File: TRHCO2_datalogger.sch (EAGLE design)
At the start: 32 parts, among them J3 MicroUSB (5V), U1 ATMEGA328P-MU, U7 SHT31/35, U8 MCP1703/3.3V, Y1 16MHZ

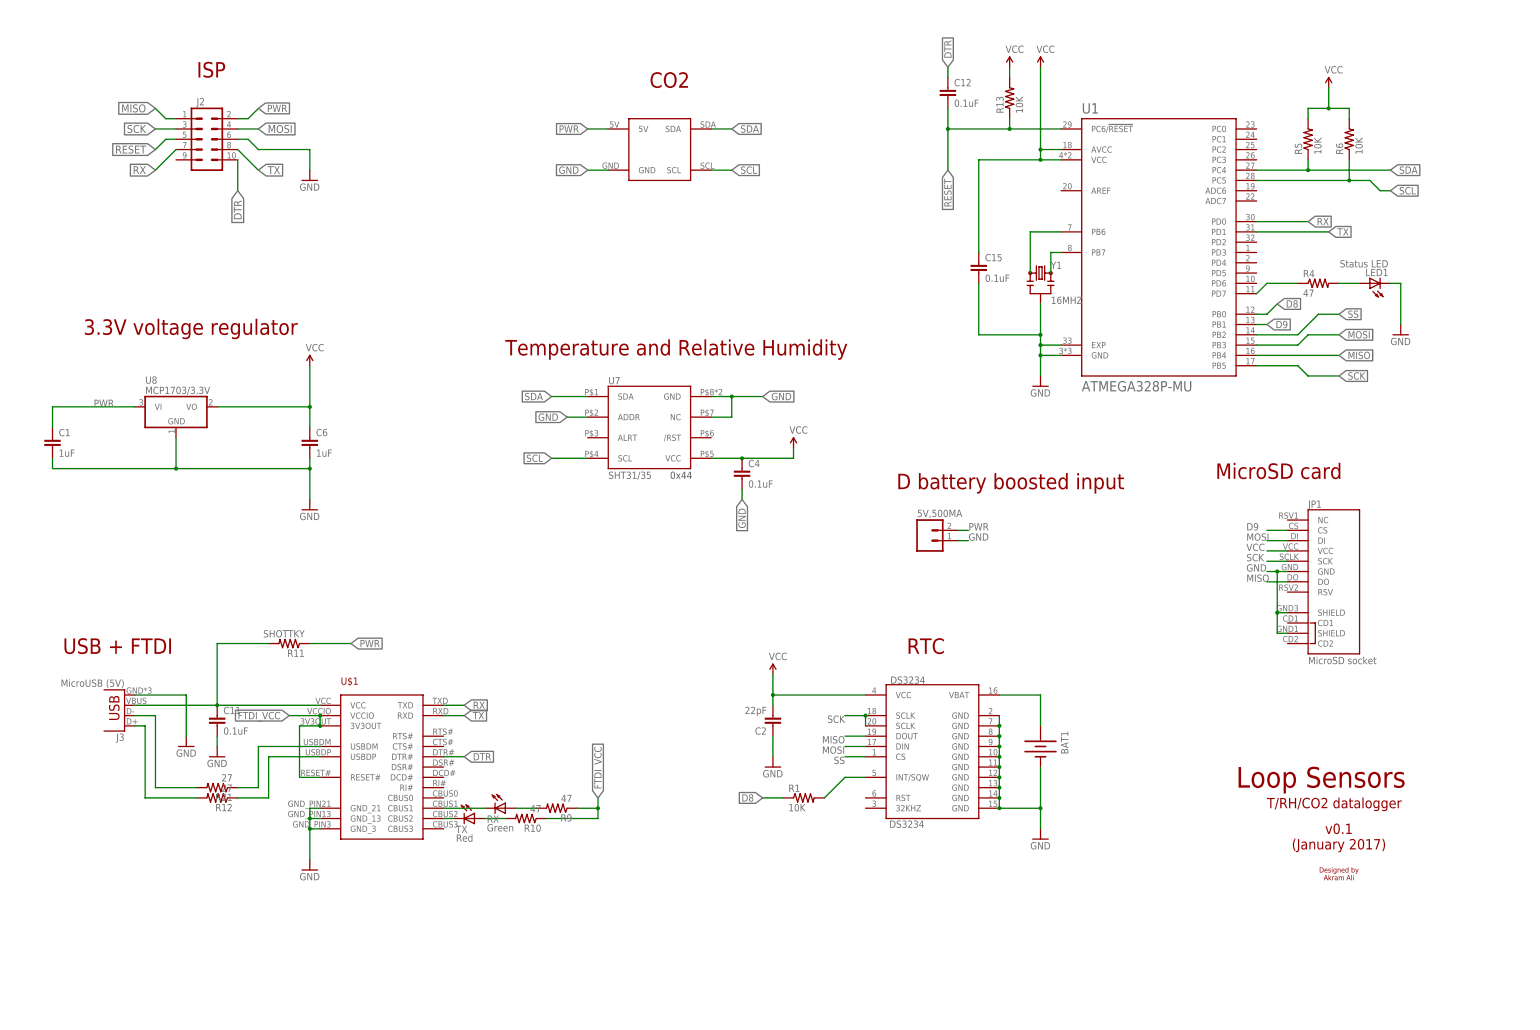
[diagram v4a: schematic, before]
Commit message: v0.2 - Major fixes
- Flipped header for LiPo boost. + and - are now facing up
- Added pullup on DS3234 clock - so there is no interference while
flashing bootloader (can be removed by desoldering jumper)
- Added NPN transistor in the circuit to switch microSD card on/off for
previous adaptations of Sdfat library
- Routed CS pin of microSD card to ISP header for debug when necessary
- Added 1uF capacitor to microSD's supply
- Minor bug fixes and trace rearrangments
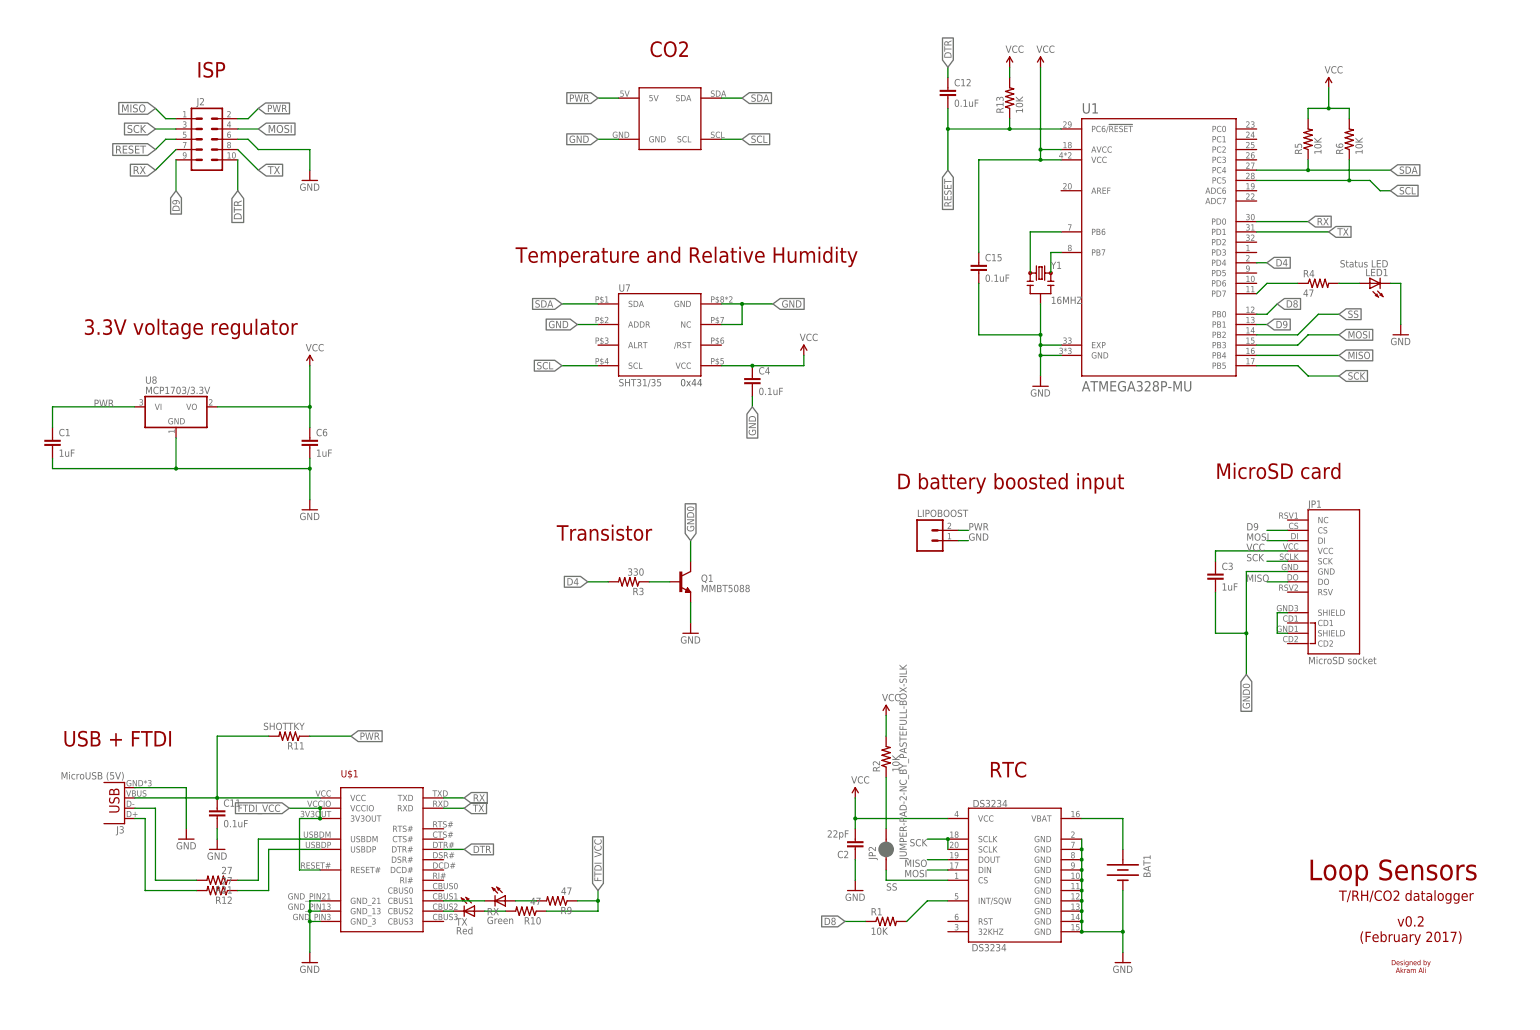
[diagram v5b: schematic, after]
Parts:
- added C3: 1uF, SparkFun-Capacitors:CAP0805
- added JP2: JUMPER-PAD-2-NC_BY_PASTEFULL-BOX-SILK, SparkFun-Passives:JUMPER-PAD-2-NC_BY_PASTEFULL-BOX-SILK
- added Q1: MMBT5088, SparkFun-DiscreteSemi:TRANSISTOR_NPNMMBT5088
- added R2: 10K, SparkFun-Resistors:RESISTOR0805-RES
- added R3: 330, SparkFun-Passives:RESISTOR0805-RES
- renumbered 5V,500MA to LIPOBOOST
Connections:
- new net D4: R3.2, U1.PD4
- new net GND0: C3.2, JP1.GND, Q1.C
- new net N$6: Q1.B, R3.1
- new net N$7: JP2.2, R2.1
- net D9: now also J2.9
- net GND: now also Q1.E; no longer JP1.GND
- net SS: now also JP2.1
- net VCC: now also C3.1, R2.2
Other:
- note added: "Transistor"
- note added: "v0.2 (February 2017)"
- note removed: "v0.1 (January 2017)"
- moved on the sheet: BAT1, C11, C2, C4, DS3234, J3, R1, R10, R11, R12, R21, R9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

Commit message: v0.3 - major update
- Added boost converter (TPS61090)
- Added switch for battery
- Replaced ISP header with TagConnect pins
- Added pullups on all SPI devices
- Removed transistor from sensors and SD card
- Removed jumper @ DS3234 pull up
- Battery groove at edge
- Added LEDs for status indication
- Changed CO2 sensor dimensions to be exact
- Align USB port in center
- Removed PWR LED from booster circuir
- Changed some parts to 0402
- Replaced 16 MHz footprint
- Reroute all traces
- Added LiPo charger circuit (MCP73871)
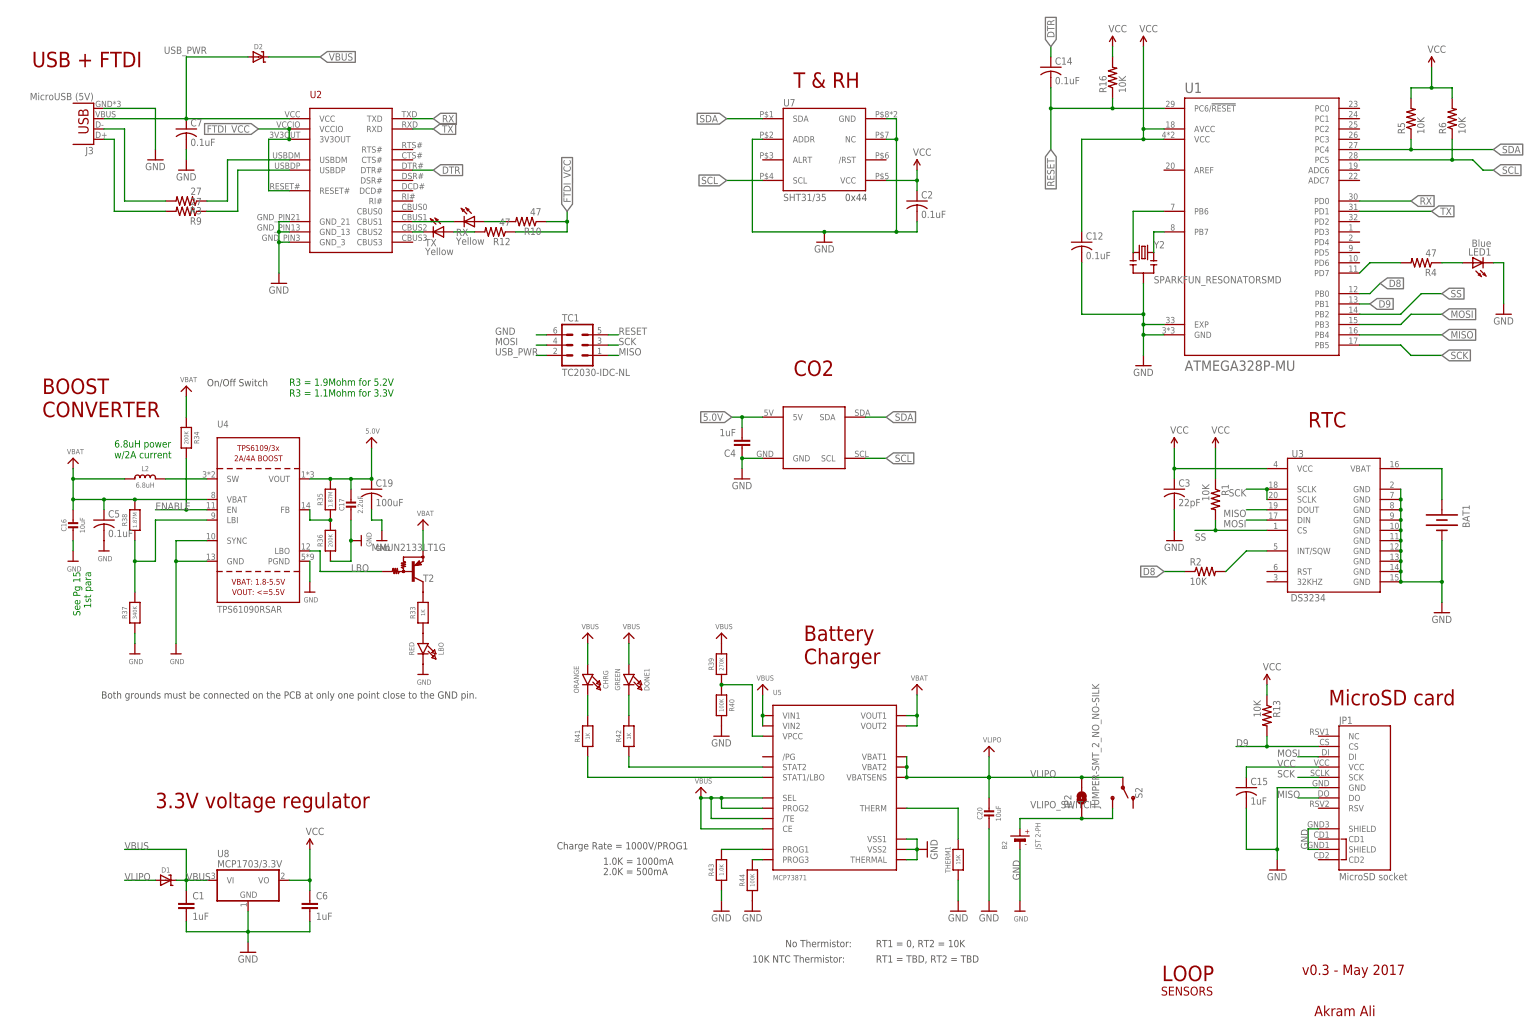
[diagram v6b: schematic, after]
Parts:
- removed C11: 0.1uF, SparkFun-Capacitors:CAP0805
- removed DS3234: DS3234, SparkFun-FreqCtrl:DS3234
- removed J2: (no value), SparkFun-Connectors:M05X2PTH
- removed LIPOBOOST: (no value), SparkFun-Connectors:M02PTH
- removed Q1: MMBT5088, SparkFun-DiscreteSemi:TRANSISTOR_NPNMMBT5088
- removed R11: SHOTTKY, SparkFun-Passives:RESISTOR0805-RES
- removed R21: 27, SparkFun-Passives:RESISTOR0805-RES
- removed U$1: FT231XQ-R, ftdi_ft231xq-r:FT231XQ-R
- removed U$3: K30-CO2-I2C, K30-CO2-I2C:K30-CO2-I2C
- removed Y1: 16MHZ, SparkFun-FreqCtrl:RESONATOR16MHZ
- added B2: JST 2-PH, microbuilder:BATTERY
- added C14, C5, C7: 0.1uF, adafruit:C-USC0402
- added C16, C20: 10uF, microbuilder:CAP_CERAMIC0805-NOOUTLINE
- added C17: 2.2uF, microbuilder:CAP_CERAMIC0805-NOOUTLINE
- added C19: 100uF, rcl:C-USC1210
- added CHRG: ORANGE, microbuilder:LED0805_NOOUTLINE
- added D1, D2: (no value), Adafruit Feather 32u4 Bluefruit LE:MICROBUILDER_DIODE-SCHOTTKYSOD-123
- added DONE1: GREEN, microbuilder:LED0805_NOOUTLINE
- added L2: 6.8uH, microbuilder:INDUCTORTDK_VLC5045
- added LBO: RED, microbuilder:LED0805_NOOUTLINE
- added R16: 10K, adafruit:R-US_R0402
- added R33, R41, R42: 1K, microbuilder:RESISTOR0805_NOOUTLINE
- added R34, R36: 200K, microbuilder:RESISTOR0805_NOOUTLINE
- added R35: 1.87M, microbuilder:RESISTOR0805_NOOUTLINE
- added R37: 340K, microbuilder:RESISTOR_0805MP
- added R38: 1.87M, microbuilder:RESISTOR_0805MP
- added R39: 270K, microbuilder:RESISTOR0805_NOOUTLINE
- added R40, R44: 100K, microbuilder:RESISTOR0805_NOOUTLINE
- added R43: 1.0K, microbuilder:RESISTOR0805_NOOUTLINE
- added S2: (no value), SparkFun-Switches:SWITCH-SPDT-SMD-RIGHT-ANGLE
- added T2: MMUN2133LT1G, transistor:MUN2114T1-PNP_DRIVER-SC59-BEC
- added TC1: TC2030-IDC-NL, TagConnect:TC2030-IDC-NL
- added THERM1: 15K, microbuilder:RESISTOR0805_NOOUTLINE
- added U2: FT231XQ-R, ftdi_ft231xq-r:FT231XQ-R
- added U3: DS3234, SparkFun-FreqCtrl:DS3234
- added U4: TPS61090RSAR, microbuilder:VREG_TPS6103X
- added U5: MCP73871, microbuilder:MCP73871
- added U6: K30-CO2-I2C, K30-CO2-I2C:K30-CO2-I2C
- added Y2: SPARKFUN_RESONATORSMD, Adafruit Feather 32u4 Bluefruit LE:SPARKFUN_RESONATORSMD
- C12: device SparkFun-Passives:CAP0805 -> adafruit:C-USC0402; MPN AC0805KRX7R9BB104 -> (none)
- C15: value 0.1uF -> 1uF; device SparkFun-Passives:CAP0805 -> adafruit:C-USC0402; MPN AC0805KRX7R9BB104 -> (none)
- C2: value 22pF -> 0.1uF; device SparkFun-Passives:CAP0805 -> adafruit:C-USC0402; MPN AC0805KRX7R9BB104 -> (none)
- C3: value 1uF -> 22pF; device SparkFun-Capacitors:CAP0805 -> adafruit:C-USC0402; MPN CC0805KKX7R7BB105 -> (none)
- C4: value 0.1uF -> 1uF; device SparkFun-Passives:CAP0805 -> SparkFun-Capacitors:CAP0805; MPN AC0805KRX7R9BB104 -> CC0805KKX7R7BB105
- JP2: value JUMPER-PAD-2-NC_BY_PASTEFULL-BOX-SILK -> JUMPER-SMT_2_NO_NO-SILK; device SparkFun-Passives:JUMPER-PAD-2-NC_BY_PASTEFULL-BOX-SILK -> SparkFun-Jumpers:JUMPER-SMT_2_NO_NO-SILK
- LED1: value Status LED -> Blue
- R1, R4: device SparkFun-Resistors:RESISTOR0805-RES -> adafruit:R-US_R0402; MPN RC0805JR-0747RL -> (none)
- R10: device SparkFun-Passives:RESISTOR0805-RES -> adafruit:R-US_R0402; MPN RC0805JR-0747RL -> (none)
- R12: value 27 -> 47; device SparkFun-Passives:RESISTOR0805-RES -> adafruit:R-US_R0402; MPN RC0805FR-0727RL -> (none)
- R13: device SparkFun-Passives:RESISTOR0805-RES -> adafruit:R-US_R0402; MPN RC0805JR-0710KL -> (none)
- R2, R5, R6: device SparkFun-Resistors:RESISTOR0805-RES -> adafruit:R-US_R0402; MPN RC0805JR-0710KL -> (none)
- R3: value 330 -> 27; device SparkFun-Passives:RESISTOR0805-RES -> adafruit:R-US_R0402; MPN RC0805JR-0710KL -> (none)
- R9: value 47 -> 27; device SparkFun-Passives:RESISTOR0805-RES -> adafruit:R-US_R0402; MPN RC0805JR-0747RL -> (none)
- RX: value Green -> Yellow
- TX: value Red -> Yellow
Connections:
- removed net D4: R3.2, U1.PD4
- removed net GND0: C3.2, JP1.GND, Q1.C
- removed net PWR: C1.1, J2.2, LIPOBOOST.2, R11.1, U$3.5V, U8.VI
- new net 5.0V: C17.1, C19.1, C4.2, R35.2, U4.VOUT, U6.5V
- new net ENABLE: R34.2, U4.EN
- new net LBO: T2.B, U4.LBO
- new net N$14: LBO.A, R33.1
- new net N$28: R35.1, R36.2, U4.FB
- new net N$30: R33.2, T2.C
- new net N$31: R39.1, R40.1, U5.VPCC
- new net N$34: R42.1, U5.STAT2
- new net N$35: R41.1, U5.STAT1/LBO
- new net N$36: R43.2, U5.PROG1
- new net N$37: THERM1.2, U5.THERM
- new net N$38: DONE1.C, R42.2
- new net N$39: CHRG.C, R41.2
- new net N$40: R44.2, U5.PROG3
- new net USB_PWR: C7.1, D2.A, J3.VBUS, TC1.2, U2.VCC
- new net VBAT: C16.1, C5.1, L2.1, R34.1, R38.2, T2.E, U4.VBAT, U5.VOUT1, U5.VOUT2
- new net VLIPO: C20.1, D1.A, JP2.2, S2.P, U5.VBAT1, U5.VBAT2, U5.VBATSENS
- new net VLIPO_SWITCH: B2.+, JP2.1, S2.S
- net D8: now also R2.1; no longer R1.1
- net D9: now also R13.2; no longer J2.9
- net DTR: now also C14.1, U2.DTR#; no longer C12.1, J2.10, U$1.DTR#
- net FTDI_VCC: now also R12.1, U2.3V3OUT, U2.RESET#, U2.VCCIO; no longer R9.1, U$1.3V3OUT, U$1.RESET#, U$1.VCCIO
- net GND: now also B2.-, C12.2, C16.2, C17.2, C19.2, C2.2, C20.2, C3.2, C4.1, C5.2, C7.2, JP1.GND, LBO.C, R36.1, R37.1, R40.2, R43.1, R44.1, TC1.6, THERM1.1, U2.GND_13, U2.GND_21, U2.GND_3, U3.GND, U3.GND@10, U3.GND@11, U3.GND@12, U3.GND@13, U3.GND@14, U3.GND@2, U3.GND@7, U3.GND@8, U3.GND@9, U4.GND, U4.PGND, U4.SYNC, U5.THERMAL, U5.VSS1, U5.VSS2, U6.GND, Y2.2; no longer C11.2, C2.1, C4.2, DS3234.GND, DS3234.GND@10, DS3234.GND@11, DS3234.GND@12, DS3234.GND@13, DS3234.GND@14, DS3234.GND@2, DS3234.GND@7, DS3234.GND@8, DS3234.GND@9, J2.6, LIPOBOOST.1, Q1.E, U$1.GND_13, U$1.GND_21, U$1.GND_3, U$3.GND, Y1.2
- net MISO: now also TC1.1, U3.DOUT; no longer DS3234.DOUT, J2.1
- net MOSI: now also TC1.4, U3.DIN; no longer DS3234.DIN, J2.4
- net N$1: now also R4.2; no longer R4.1
- net N$17: now also U2.CBUS1; no longer U$1.CBUS1
- net N$18: now also U2.CBUS2; no longer U$1.CBUS2
- net N$2: now also R2.2, U3.INT/SQW; no longer DS3234.INT/SQW, R1.2
- net N$25: now also R3.1, U2.USBDM; no longer R21.1, U$1.USBDM
- net N$26: now also R9.1, U2.USBDP; no longer R12.1, U$1.USBDP
- net N$27: now also R10.2; no longer R9.2
- net N$29: now also R12.2; no longer R10.2
- net N$3: now also R4.1; no longer R4.2
- net N$32: now also R3.2; no longer R21.2
- net N$33: now also R9.2; no longer R12.2
- net N$4: now also Y2.3; no longer Y1.3
- net N$5: now also Y2.1; no longer Y1.1
- net N$6: now also L2.2, U4.SW; no longer Q1.B, R3.1
- net N$7: now also R37.2, R38.1, U4.LBI; no longer JP2.2, R2.1
- net N$8: now also U3.VBAT; no longer DS3234.VBAT
- net RESET: now also C14.2, R16.1, TC1.5; no longer C12.2, J2.5, R13.1
- net RX: now also U2.TXD; no longer J2.7, U$1.TXD
- net SCK: now also TC1.3, U3.SCLK@18, U3.SCLK@20; no longer DS3234.SCLK@18, DS3234.SCLK@20, J2.3
- net SCL: now also U6.SCL; no longer U$3.SCL
- net SDA: now also U6.SDA; no longer U$3.SDA
- net SS: now also R1.2, U3.CS; no longer DS3234.CS, JP2.1
- net TX: now also U2.RXD; no longer J2.8, U$1.RXD
- net VBUS: now also C1.1, CHRG.A, D1.C, D2.C, DONE1.A, R39.2, U5./TE, U5.CE, U5.PROG2, U5.SEL, U5.VIN1, U5.VIN2, U8.VI; no longer C11.1, J3.VBUS, R11.2, U$1.VCC
- net VCC: now also C12.1, C2.1, R1.1, R13.1, R16.2, U3.VCC; no longer C2.2, C4.1, DS3234.VCC, R13.2, R2.2
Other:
- note added: "1.0K = 1000mA"
- note added: "10K NTC Thermistor:"
- note added: "2.0K = 500mA"
- note added: "6.8uH power w/2A current"
- note added: "Akram Ali"
- note added: "BOOST CONVERTER"
- note added: "Battery Charger"
- note added: "Both grounds must be connected on the PCB at only one point close to the GND pin."
- note added: "Charge Rate = 1000V/PROG1"
- note added: "LOOP"
- note added: "No Thermistor:"
- note added: "On/Off Switch"
- note added: "R3 = 1.9Mohm for 5.2V R3 = 1.1Mohm for 3.3V"
- note added: "RT1 = 0, RT2 = 10K"
- note added: "RT1 = TBD, RT2 = TBD"
- note added: "SENSORS"
- note added: "See Pg 15 1st para"
- note added: "T & RH"
- note added: "v0.3 - May 2017"
- note removed: "D battery boosted input"
- note removed: "Designed by Akram Ali"
- note removed: "ISP"
- note removed: "Loop Sensors"
- note removed: "T/RH/CO2 datalogger"
- note removed: "Temperature and Relative Humidity"
- note removed: "Transistor"
- note removed: "v0.2 (February 2017)"
- moved on the sheet: BAT1, C1, C12, C15, C2, C3, C4, C6, J3, JP1, LED1, R1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
